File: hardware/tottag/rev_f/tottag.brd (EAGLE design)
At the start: 61 x 34.5 mm, 157 parts, among them J1 MICRO_USB_B_HIROSE_ZX62-B-5PA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, J2 CON_MICRO_SDDM3AT-SF-PEJM5, J3 BAT_HOLE, J4 TC2030-JLINK-NL, J5 TC2030-JLINK-NL, T1 HHM1595A1, U1 DW1000, U10 STM32F091CC, U11 AB1815-T3, U2 FT232RQ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

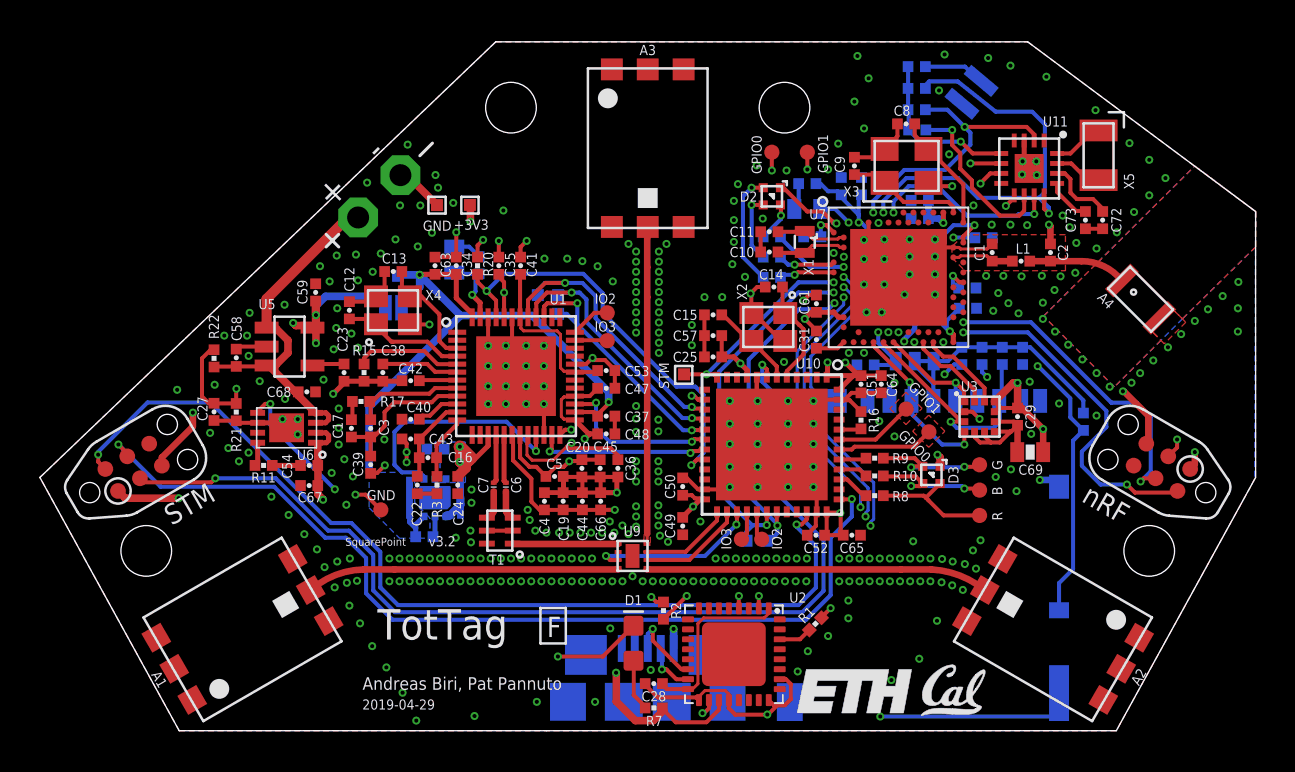
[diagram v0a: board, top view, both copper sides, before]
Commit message: fix capacitor, resistor numbering
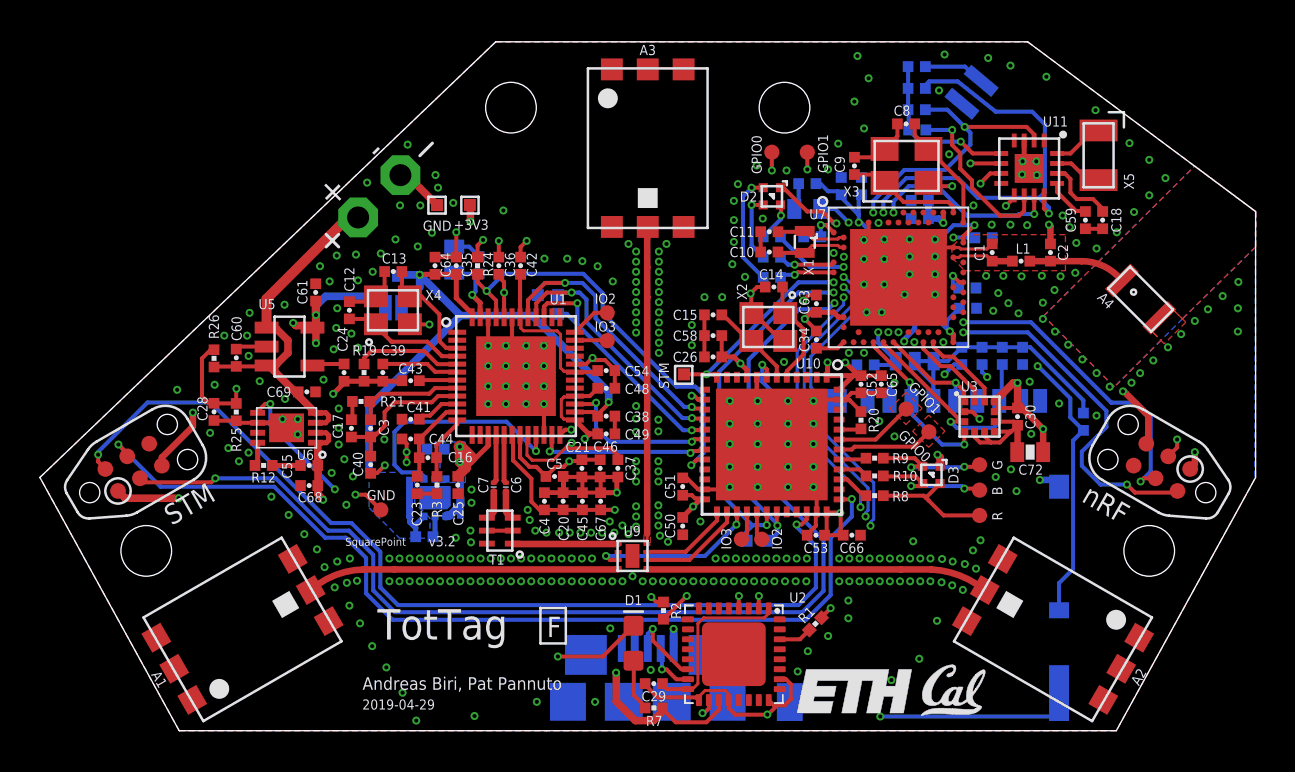
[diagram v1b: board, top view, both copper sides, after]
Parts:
- C18: value 100pF -> 47pF
- C19: value 330pF -> 100pF
- C21: value 820pF -> 330pF
- C23: value 10nF -> 820pF
- C26: value 47nF -> 10nF
- C27: value 0.1uF -> 47nF
- C54: value 1uF -> 0.1uF
- C58, C59: value 4.7uF -> 1uF
- C69: value 10uF -> 4.7uF; device passives:0603_CAP -> passives:0402_CAP
- C70: value 10uF -> 4.7uF
- C71: value 47uF -> 10uF; device passives:0603_CAP -> passives:0402_CAP
- C72: value 47pF -> 10uF; device passives:0402_CAP -> passives:0603_CAP
- C73: value 1uF -> 47uF; device passives:0402_CAP -> passives:0603_CAP
- R11: value 2k 1% -> 1.41k
- R12: value 10k -> 2k 1%
- R15: value 11k 1% -> 10k
- R16: value 11k -> 10k
- R17: value 16k -> 10k
- R18: value 100k -> 10k
- R19: value 100k -> 11k 1%
- R20: value 100k -> 11k
- R21: value 2.2M -> 16k
- R22: value 10M -> 100k
- R23: value 10k -> 100k
- R24: value 1.41k -> 100k
- R25: value 10k -> 2.2M
- R26: value 10k -> 10M
- moved C60 39.4 mm to (-20.6, 14.9), flipped to the top, turned to 90 degrees
- moved C59 38.8 mm to (21.9, 21.8), turned to 270 degrees
- moved R11 38.4 mm to (13.5, 29.5), flipped to the bottom
- moved R26 37.7 mm to (-21.7, 14.9), flipped to the top, turned to 270 degrees
- moved R25 37.3 mm to (-20.6, 12.2), flipped to the top, turned to 90 degrees
- moved C69 36.4 mm to (-17.1, 13.2), turned to 0 degrees
- moved R19 36.2 mm to (-14.2, 14.1), flipped to the top
- moved R12 35.4 mm to (-19.3, 9.49), flipped to the top, turned to 180 degrees
- moved C27 34.4 mm to (10.7, 23.5), flipped to the bottom
- moved C55 33.4 mm to (-17.0, 9.49), flipped to the top, turned to 180 degrees
- moved R22 32.7 mm to (10.9, 14.5), flipped to the bottom, turned to 0 degrees
- moved R15 32.0 mm to (17.8, 15.0), flipped to the bottom
- moved C73 31.7 mm to (-9.70, 19.8), flipped to the bottom, turned to 90 degrees
- moved R17 31.5 mm to (13.5, 27.3), flipped to the bottom, turned to 0 degrees
- moved C62 29.8 mm to (18.8, 15.0), turned to 270 degrees
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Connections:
- net !NRF_CS_RTC: now also R18.1; no longer R26.1
- net !NRF_CS_SD: now also R14.1; no longer R13.1
- net !SD_DETECT: now also R23.1; no longer R19.1
- net +1V8: now also C35.1, C38.1, C64.1, C71.1; no longer C34.1, C37.1, C63.1, C70.1
- net +3V3: now also C21.1, C26.1, C34.1, C53.1, C56.1, C58.1, C63.1, C67.1, C70.1, C72.1, C73.1; no longer C19.1, C24.1, C29.1, C44.1, C55.1, C57.1, C59.1, C62.1, C64.1, C69.1, C71.1
- net BATIN: now also C28.2, R25.2, R26.1; no longer C27.2, R21.2, R22.1
- net DW_IRQ: now also R24.2; no longer R20.2
- net GND: now also C22.2, C27.2, C28.1, R12.1, R19.1, R20.2, R22.2, R24.1, R25.1; no longer C23.2, C27.1, C28.2, R11.1, R15.1, R16.2, R18.2, R20.1, R21.1
- net N$1: now also C29.1; no longer C28.1
- net N$10: now also C19.1; no longer C18.1
- net N$11: now also C24.1; no longer C23.1
- net N$12: now also R21.2; no longer R17.2
- net N$13: now also R12.2; no longer R11.2
- net N$16: now also R21.1; no longer R17.1
- net N$2: now also C22.1; no longer C21.1
- net N$21: now also R19.2; no longer R15.2
- net N$22: now also R20.1; no longer R16.1
- net N$35: now also C18.1; no longer C72.1
- net N$43: now also R16.1; no longer R23.1
- net N$45: now also R11.2; no longer R24.2
- net N$55: now also C62.1, R15.2, R23.2; no longer C60.1, R12.2, R19.2
- net N$8: now also C23.1; no longer C22.1
- net N$9: now also C27.1, C57.1; no longer C26.1, C56.1
- net NRF_MISO: now also R15.1; no longer R14.1
- net NRF_MOSI: now also R13.1; no longer R12.1
- net RTC_WDI: now also R17.1; no longer R25.1
- net SD_EN: now also R22.1; no longer R18.1
- net VBAT: now also C60.1, C69.1, R26.2; no longer C58.1, C68.1, R22.2
- net VBAT_RTC: now also R11.1, R16.2, R17.2, R18.2; no longer R23.2, R24.1, R25.2, R26.2
- net VCC: now also C59.1; no longer C73.1
- net VDDCLK: now also C40.1; no longer C39.1
- net VDDDIG: now also C37.1; no longer C35.1
- net VDDIF: now also C43.1; no longer C42.1
- net VDDIO: now also C42.1, C54.1; no longer C41.1, C53.1
- net VDDMS: now also C39.1; no longer C38.1
- net VDDSYN: now also C41.1; no longer C40.1
- net VDDVCO: now also C23.2, C44.1; no longer C22.2, C43.1
- net VUSB: now also C55.1, C68.1; no longer C54.1, C67.1
